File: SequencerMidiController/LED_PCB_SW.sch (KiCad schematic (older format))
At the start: 1 part, among them U1 PCB-SPST_RGB-LED-Counter-Cloc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

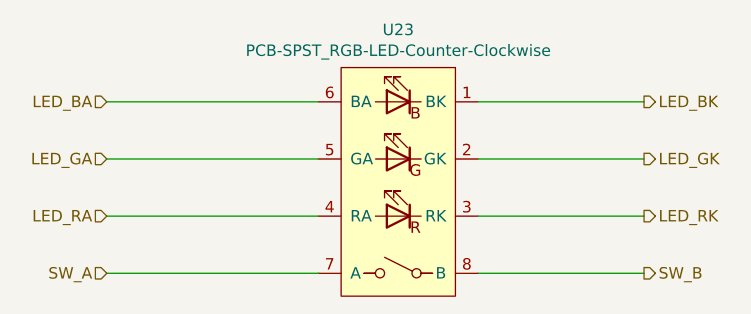
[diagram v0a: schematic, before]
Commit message: RevA Layout draft completed
- Needs tidy up
- Add test points
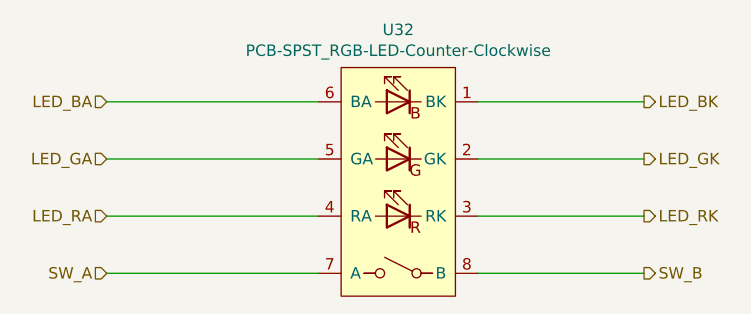
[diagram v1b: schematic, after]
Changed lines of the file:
@@
 $Descr A4 11693 8268
 encoding utf-8
-Sheet 36 46
+Sheet 40 46
 Title "Combined RGB LED and SPST"
 Date "2021-06-05"
@@
 AR Path="/60BCDD64/684F2E67/60B6A70A" Ref="U32"  Part="1"
 AR Path="/60BCDD64/684F2E71/60B6A70A" Ref="U28"  Part="1"
-F 0 "U23" H 6225 4515 50  0000 C CNN
+F 0 "U32" H 6225 4515 50  0000 C CNN
 F 1 "PCB-SPST_RGB-LED-Counter-Clockwise" H 6225 4424 50  0000 C CNN
 F 2 "PCB_SW_LED:Circular_3mm_10mm_Cree_PLLC6_CLY6D-FKC-CK1N1D1BB7D3D3" H 6225 4450 50  0001 C CNN
-F 3 "" H 6225 4450 50  0001 C CNN
+F 3 "https://www.mouser.co.uk/datasheet/2/723/1321_CLY6D_FKC-2298229.pdf" H 6225 4450 50  0001 C CNN
+F 4 "~" H 6225 3850 50  0001 C CNN "LcscNo"
+F 5 "~" H 6225 3850 50  0001 C CNN "Type"
 	1    6225 3850
 	-1   0    0    -1

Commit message: updated
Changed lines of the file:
@@
 $Descr A4 11693 8268
 encoding utf-8
-Sheet 31 46
+Sheet 16 46
 Title "Combined RGB LED and SPST"
 Date "2021-06-05"
@@
 AR Path="/60BCDD64/684F2E67/60B6A70A" Ref="U32"  Part="1"
 AR Path="/60BCDD64/684F2E71/60B6A70A" Ref="U28"  Part="1"
-F 0 "U32" H 6225 4515 50  0000 C CNN
+F 0 "U2" H 6225 4515 50  0000 C CNN
 F 1 "PCB-SPST_RGB-LED-Counter-Clockwise" H 6225 4424 50  0000 C CNN
 F 2 "PCB_SW_LED:Circular_3mm_10mm_Cree_PLLC6_CLY6D-FKC-CK1N1D1BB7D3D3" H 6225 4450 50  0001 C CNN
